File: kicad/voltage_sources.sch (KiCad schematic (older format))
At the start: 51 parts, among them Q5 BSH205, Q6 IRLML6244, Q7 BSH205, Q8 IRLML6244, U1 TPS61041, U10 TPS71533DCKR, U11 TPS61041, U2 LM2611, U3 LM2611

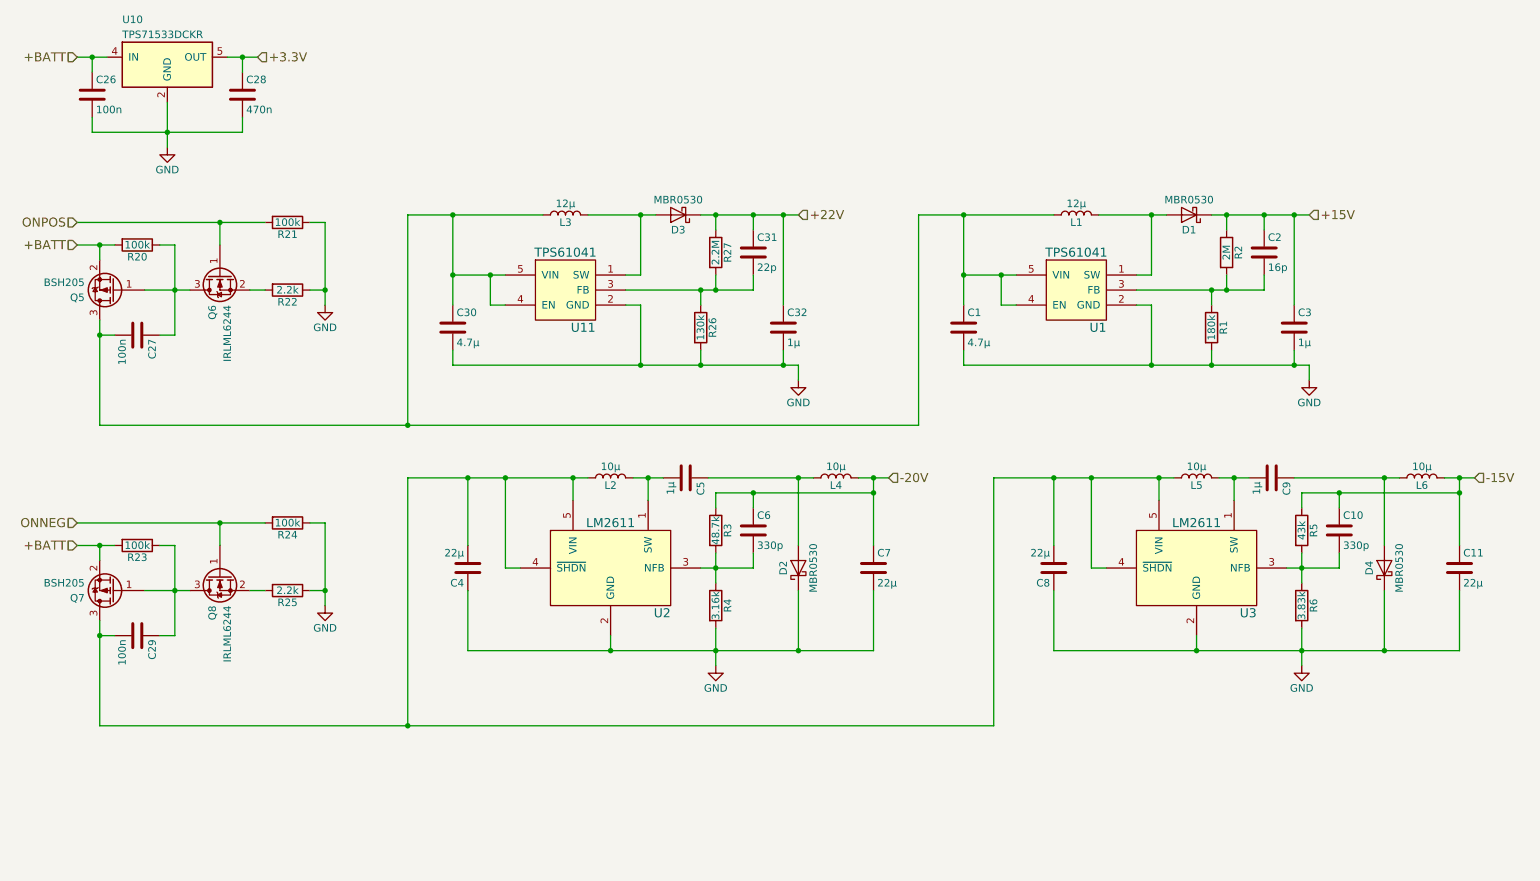
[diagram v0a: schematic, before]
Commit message: Finish schematic
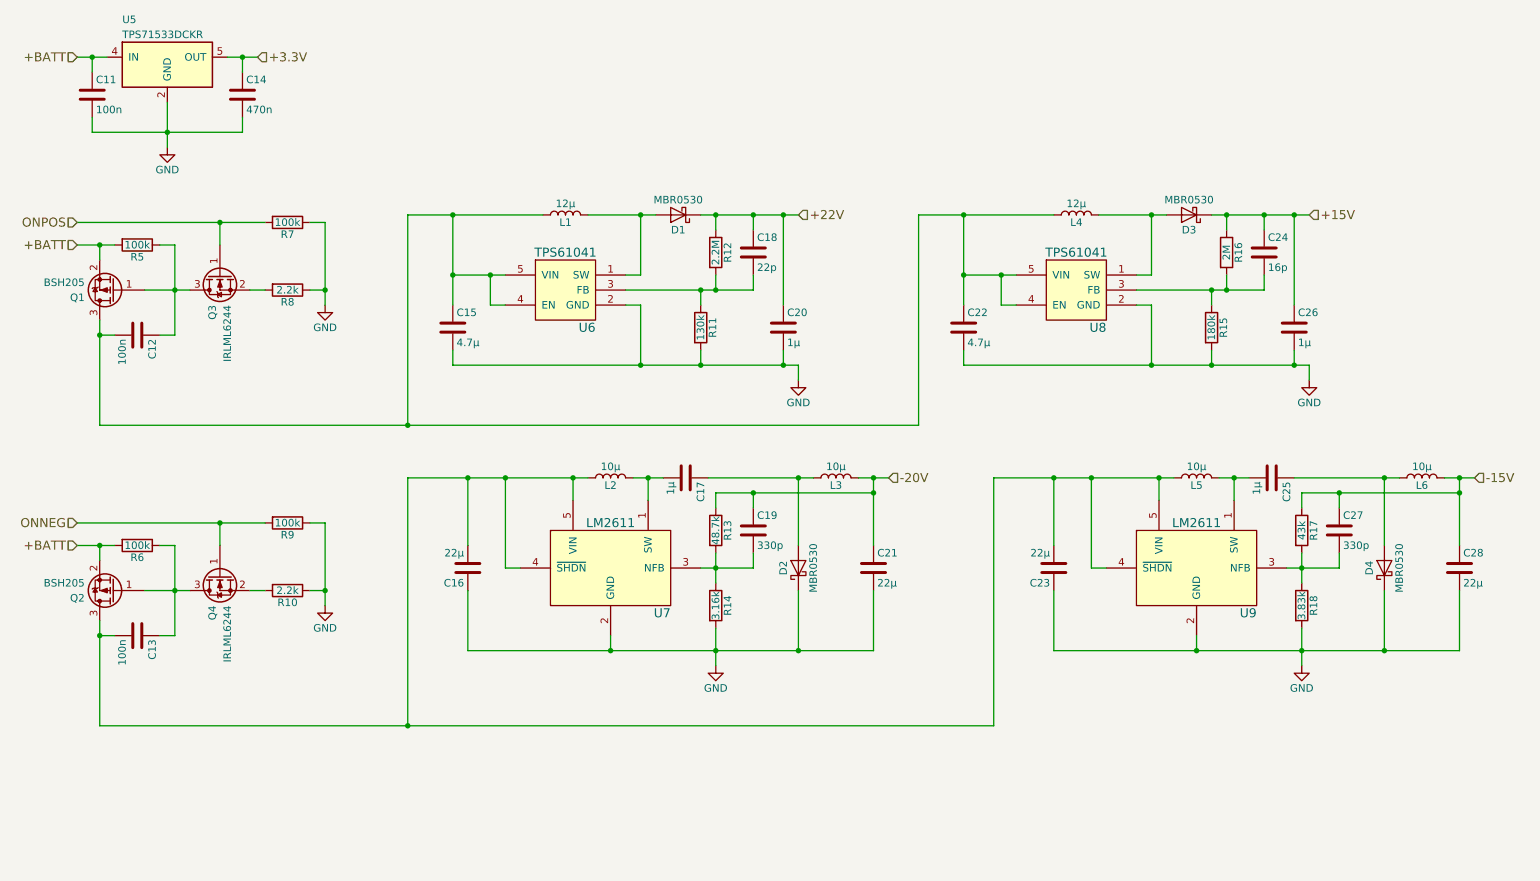
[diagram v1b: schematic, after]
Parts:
- renumbered C26 to C11, C27 to C12, C29 to C13, C28 to C14, C30 to C15, C4 to C16, C5 to C17, C31 to C18, C6 to C19, C32 to C20, C7 to C21, C1 to C22, C8 to C23, C2 to C24, C9 to C25, C3 to C26, C10 to C27, C11 to C28, D3 to D1, D1 to D3, L3 to L1, L4 to L3, L1 to L4, Q5 to Q1, Q7 to Q2, Q6 to Q3, Q8 to Q4, R25 to R10, R26 to R11, R27 to R12, R3 to R13, R4 to R14, R1 to R15, R2 to R16, R5 to R17, R6 to R18, R20 to R5, R23 to R6, R21 to R7, R22 to R8, R24 to R9, U10 to U5, U11 to U6, U2 to U7, U1 to U8, U3 to U9

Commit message: Set most footprints
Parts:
- C11, C12, C13, C14, C15, C16, C17, C18, C19, C20, C21, C22, C23, C24, C25, C26, C27, C28: footprint (none) -> Capacitors_SMD:C_0805_HandSoldering
- D1, D2, D3, D4: footprint (none) -> Diodes_SMD:D_SOD-123
- Q1, Q2, Q3, Q4: footprint (none) -> TO_SOT_Packages_SMD:SOT-23_Handsoldering
- R10, R11, R12, R13, R14, R15, R16, R17, R18, R5, R6, R7, R8, R9: footprint (none) -> Resistors_SMD:R_0805_HandSoldering
- U5: footprint (none) -> TO_SOT_Packages_SMD:SOT-353_SC-70-5_Handsoldering
- U6, U7, U8, U9: footprint (none) -> TO_SOT_Packages_SMD:SOT-23-5_HandSoldering

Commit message: Finish footprints
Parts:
- L1, L4: footprint (none) -> einkclock:Bourns_Inductor_SDR0703
- L2, L3, L5, L6: footprint (none) -> einkclock:Inductor_TAIYO_YUDEN_3225
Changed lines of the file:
@@
 F 0 "L1" V 4150 1950 50  0000 C CNN
 F 1 "12µ" V 4275 1950 50  0000 C CNN
-F 2 "" H 4200 1950 50  0001 C CNN
+F 2 "einkclock:Bourns_Inductor_SDR0703" H 4200 1950 50  0001 C CNN
 F 3 "" H 4200 1950 50  0000 C CNN
 	1    4200 1950
@@
 F 0 "L4" V 7550 1950 50  0000 C CNN
 F 1 "12µ" V 7675 1950 50  0000 C CNN
-F 2 "" H 7600 1950 50  0001 C CNN
+F 2 "einkclock:Bourns_Inductor_SDR0703" H 7600 1950 50  0001 C CNN
 F 3 "" H 7600 1950 50  0000 C CNN
 	1    7600 1950
@@
 F 0 "L2" V 4450 3700 50  0000 C CNN
 F 1 "10µ" V 4575 3700 50  0000 C CNN
-F 2 "" H 4500 3700 50  0001 C CNN
+F 2 "einkclock:Inductor_TAIYO_YUDEN_3225" H 4500 3700 50  0001 C CNN
 F 3 "" H 4500 3700 50  0000 C CNN
 	1    4500 3700
@@
 F 0 "L3" V 5950 3700 50  0000 C CNN
 F 1 "10µ" V 6075 3700 50  0000 C CNN
-F 2 "" H 6000 3700 50  0001 C CNN
+F 2 "einkclock:Inductor_TAIYO_YUDEN_3225" H 6000 3700 50  0001 C CNN
 F 3 "" H 6000 3700 50  0000 C CNN
 	1    6000 3700
@@
 F 0 "L5" V 8350 3700 50  0000 C CNN
 F 1 "10µ" V 8475 3700 50  0000 C CNN
-F 2 "" H 8400 3700 50  0001 C CNN
+F 2 "einkclock:Inductor_TAIYO_YUDEN_3225" H 8400 3700 50  0001 C CNN
 F 3 "" H 8400 3700 50  0000 C CNN
 	1    8400 3700
@@
 F 0 "L6" V 9850 3700 50  0000 C CNN
 F 1 "10µ" V 9975 3700 50  0000 C CNN
-F 2 "" H 9900 3700 50  0001 C CNN
+F 2 "einkclock:Inductor_TAIYO_YUDEN_3225" H 9900 3700 50  0001 C CNN
 F 3 "" H 9900 3700 50  0000 C CNN
 	1    9900 3700

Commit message: First routing
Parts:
- C11, C12, C13, C14, C15, C16, C17, C18, C19, C20, C21, C22, C23, C24, C25, C26, C27, C28: footprint Capacitors_SMD:C_0805_HandSoldering -> Resistors_SMD:R_0805_HandSoldering
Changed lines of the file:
@@
 F 0 "C11" H 1075 1250 50  0000 L CNN
 F 1 "100n" H 1075 1050 50  0000 L CNN
-F 2 "Capacitors_SMD:C_0805_HandSoldering" H 1088 1000 50  0001 C CNN
+F 2 "Resistors_SMD:R_0805_HandSoldering" H 1088 1000 50  0001 C CNN
 F 3 "" H 1050 1150 50  0000 C CNN
 	1    1050 1150
@@
 F 0 "C14" H 2075 1250 50  0000 L CNN
 F 1 "470n" H 2075 1050 50  0000 L CNN
-F 2 "Capacitors_SMD:C_0805_HandSoldering" H 2088 1000 50  0001 C CNN
+F 2 "Resistors_SMD:R_0805_HandSoldering" H 2088 1000 50  0001 C CNN
 F 3 "" H 2050 1150 50  0000 C CNN
 	1    2050 1150
@@
 F 0 "C12" H 1375 2850 50  0000 L CNN
 F 1 "100n" H 1375 2650 50  0000 L CNN
-F 2 "Capacitors_SMD:C_0805_HandSoldering" H 1388 2600 50  0001 C CNN
+F 2 "Resistors_SMD:R_0805_HandSoldering" H 1388 2600 50  0001 C CNN
 F 3 "" H 1350 2750 50  0000 C CNN
 	1    1350 2750
@@
 F 0 "C13" H 1375 4850 50  0000 L CNN
 F 1 "100n" H 1375 4650 50  0000 L CNN
-F 2 "Capacitors_SMD:C_0805_HandSoldering" H 1388 4600 50  0001 C CNN
+F 2 "Resistors_SMD:R_0805_HandSoldering" H 1388 4600 50  0001 C CNN
 F 3 "" H 1350 4750 50  0000 C CNN
 	1    1350 4750
@@
 F 0 "C15" H 3475 2800 50  0000 L CNN
 F 1 "4.7µ" H 3475 2600 50  0000 L CNN
-F 2 "Capacitors_SMD:C_0805_HandSoldering" H 3488 2550 50  0001 C CNN
+F 2 "Resistors_SMD:R_0805_HandSoldering" H 3488 2550 50  0001 C CNN
 F 3 "" H 3450 2700 50  0000 C CNN
 	1    3450 2700
@@
 F 0 "C20" H 5675 2800 50  0000 L CNN
 F 1 "1µ" H 5675 2600 50  0000 L CNN
-F 2 "Capacitors_SMD:C_0805_HandSoldering" H 5688 2550 50  0001 C CNN
+F 2 "Resistors_SMD:R_0805_HandSoldering" H 5688 2550 50  0001 C CNN
 F 3 "" H 5650 2700 50  0000 C CNN
 	1    5650 2700
@@
 F 0 "C18" H 5475 2300 50  0000 L CNN
 F 1 "22p" H 5475 2100 50  0000 L CNN
-F 2 "Capacitors_SMD:C_0805_HandSoldering" H 5488 2050 50  0001 C CNN
+F 2 "Resistors_SMD:R_0805_HandSoldering" H 5488 2050 50  0001 C CNN
 F 3 "" H 5450 2200 50  0000 C CNN
 	1    5450 2200
@@
 F 0 "C22" H 6875 2800 50  0000 L CNN
 F 1 "4.7µ" H 6875 2600 50  0000 L CNN
-F 2 "Capacitors_SMD:C_0805_HandSoldering" H 6888 2550 50  0001 C CNN
+F 2 "Resistors_SMD:R_0805_HandSoldering" H 6888 2550 50  0001 C CNN
 F 3 "" H 6850 2700 50  0000 C CNN
 	1    6850 2700
@@
 F 0 "C26" H 9075 2800 50  0000 L CNN
 F 1 "1µ" H 9075 2600 50  0000 L CNN
-F 2 "Capacitors_SMD:C_0805_HandSoldering" H 9088 2550 50  0001 C CNN
+F 2 "Resistors_SMD:R_0805_HandSoldering" H 9088 2550 50  0001 C CNN
 F 3 "" H 9050 2700 50  0000 C CNN
 	1    9050 2700
@@
 F 0 "C24" H 8875 2300 50  0000 L CNN
 F 1 "16p" H 8875 2100 50  0000 L CNN
-F 2 "Capacitors_SMD:C_0805_HandSoldering" H 8888 2050 50  0001 C CNN
+F 2 "Resistors_SMD:R_0805_HandSoldering" H 8888 2050 50  0001 C CNN
 F 3 "" H 8850 2200 50  0000 C CNN
 	1    8850 2200
@@
 F 0 "C17" H 5025 3800 50  0000 L CNN
 F 1 "1µ" H 5025 3600 50  0000 L CNN
-F 2 "Capacitors_SMD:C_0805_HandSoldering" H 5038 3550 50  0001 C CNN
+F 2 "Resistors_SMD:R_0805_HandSoldering" H 5038 3550 50  0001 C CNN
 F 3 "" H 5000 3700 50  0000 C CNN
 	1    5000 3700
@@
 F 0 "C16" H 3575 4400 50  0000 L CNN
 F 1 "22µ" H 3575 4200 50  0000 L CNN
-F 2 "Capacitors_SMD:C_0805_HandSoldering" H 3588 4150 50  0001 C CNN
+F 2 "Resistors_SMD:R_0805_HandSoldering" H 3588 4150 50  0001 C CNN
 F 3 "" H 3550 4300 50  0000 C CNN
 	1    3550 4300
@@
 F 0 "C19" H 5475 4150 50  0000 L CNN
 F 1 "330p" H 5475 3950 50  0000 L CNN
-F 2 "Capacitors_SMD:C_0805_HandSoldering" H 5488 3900 50  0001 C CNN
+F 2 "Resistors_SMD:R_0805_HandSoldering" H 5488 3900 50  0001 C CNN
 F 3 "" H 5450 4050 50  0000 C CNN
 	1    5450 4050
@@
 F 0 "C21" H 6275 4400 50  0000 L CNN
 F 1 "22µ" H 6275 4200 50  0000 L CNN
-F 2 "Capacitors_SMD:C_0805_HandSoldering" H 6288 4150 50  0001 C CNN
+F 2 "Resistors_SMD:R_0805_HandSoldering" H 6288 4150 50  0001 C CNN
 F 3 "" H 6250 4300 50  0000 C CNN
 	1    6250 4300
@@
 F 0 "C25" H 8925 3800 50  0000 L CNN
 F 1 "1µ" H 8925 3600 50  0000 L CNN
-F 2 "Capacitors_SMD:C_0805_HandSoldering" H 8938 3550 50  0001 C CNN
+F 2 "Resistors_SMD:R_0805_HandSoldering" H 8938 3550 50  0001 C CNN
 F 3 "" H 8900 3700 50  0000 C CNN
 	1    8900 3700
@@
 F 0 "C23" H 7475 4400 50  0000 L CNN
 F 1 "22µ" H 7475 4200 50  0000 L CNN
-F 2 "Capacitors_SMD:C_0805_HandSoldering" H 7488 4150 50  0001 C CNN
+F 2 "Resistors_SMD:R_0805_HandSoldering" H 7488 4150 50  0001 C CNN
 F 3 "" H 7450 4300 50  0000 C CNN
 	1    7450 4300
@@
 F 0 "C27" H 9375 4150 50  0000 L CNN
 F 1 "330p" H 9375 3950 50  0000 L CNN
-F 2 "Capacitors_SMD:C_0805_HandSoldering" H 9388 3900 50  0001 C CNN
+F 2 "Resistors_SMD:R_0805_HandSoldering" H 9388 3900 50  0001 C CNN
 F 3 "" H 9350 4050 50  0000 C CNN
 	1    9350 4050
@@
 F 0 "C28" H 10175 4400 50  0000 L CNN
 F 1 "22µ" H 10175 4200 50  0000 L CNN
-F 2 "Capacitors_SMD:C_0805_HandSoldering" H 10188 4150 50  0001 C CNN
+F 2 "Resistors_SMD:R_0805_HandSoldering" H 10188 4150 50  0001 C CNN
 F 3 "" H 10150 4300 50  0000 C CNN
 	1    10150 4300

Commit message: Add BOM
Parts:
- C11, C12, C13: Manf# (none) -> 885012207098
- C14: Manf# (none) -> 0805YC474KAT2A
- C15, C22: Manf# (none) -> GRM21BR61E475MA12L
- C16, C21, C23, C28: Manf# (none) -> C2012X5R1V226M125AC
- C17, C20, C25, C26: Manf# (none) -> UMK212B7105KG-T
- C18: Manf# (none) -> 885012007053
- C19, C27: Manf# (none) -> 885012207083
- C24: Manf# (none) -> CC0805JRNPO9BN160
- D1, D2, D3, D4: Manf# (none) -> MBR0530
- L1, L4: Manf# (none) -> SDR0703-120KL
- L2, L3, L5, L6: Manf# (none) -> CBC3225T100KRV
- Q1, Q2: Manf# (none) -> BSH205G2R
- Q3, Q4: Manf# (none) -> IRLML6244TRPBF
- R10, R8: Manf# (none) -> ERJ-6GEYJ222V
- R11: Manf# (none) -> ERJ-6ENF1303V
- R12: Manf# (none) -> ERJ-6ENF2204V
- R13: Manf# (none) -> ERJ-6ENF4872V
- R14: Manf# (none) -> ERJ-6ENF3161V
- R15: Manf# (none) -> ERJ-6ENF1803V
- R16: Manf# (none) -> ERJ-6ENF2004V
- R17: Manf# (none) -> ERJ-6ENF4302V
- R18: Manf# (none) -> ERJ-6ENF3831V
- R5, R6, R7, R9: Manf# (none) -> AS08J1003ET
- U5: Manf# (none) -> TPS71533DCKR
- U6, U8: Manf# (none) -> TPS61041DBVR
- U7, U9: Manf# (none) -> LM2611BMF/NOPB

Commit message: Refine BOM
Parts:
- C19, C27: Manf# 885012207083 -> C0805C331J5GACTU
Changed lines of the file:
@@
 F 2 "Resistors_SMD:R_0805_HandSoldering" H 5488 3900 50  0001 C CNN
 F 3 "" H 5450 4050 50  0000 C CNN
-F 4 "885012207083" H 5450 4050 60  0001 C CNN "Manf#"
+F 4 "C0805C331J5GACTU" H 5450 4050 60  0001 C CNN "Manf#"
 	1    5450 4050
 	1    0    0    -1
@@
 F 2 "Resistors_SMD:R_0805_HandSoldering" H 9388 3900 50  0001 C CNN
 F 3 "" H 9350 4050 50  0000 C CNN
-F 4 "885012207083" H 9350 4050 60  0001 C CNN "Manf#"
+F 4 "C0805C331J5GACTU" H 9350 4050 60  0001 C CNN "Manf#"
 	1    9350 4050
 	1    0    0    -1
